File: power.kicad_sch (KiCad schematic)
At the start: 56 parts, among them J4 Conn_02x02_Counter_Clockwise, Q3 Q_NMOS, Q4 Q_NMOS, Q5 Q_NMOS, Q6 Q_NMOS, U10 CJ431, U6 TPS5430DDA, U7 TPS56A37, U8 TPS2121, U9 LDL212PV33R

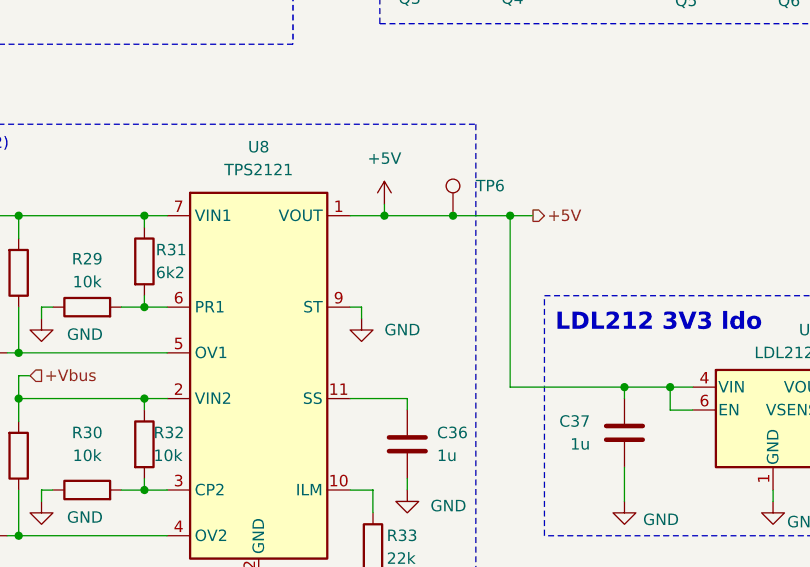
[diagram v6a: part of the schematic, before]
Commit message: schem: connect TPS2121 ST pin to MCU
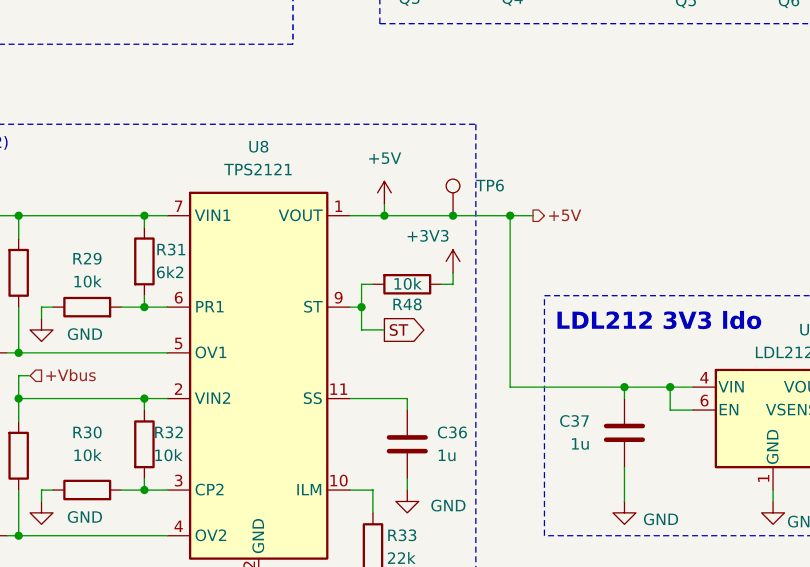
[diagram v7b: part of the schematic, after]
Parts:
- added R48: 10k, Resistor_SMD:R_0402_1005Metric, symbol Device:R
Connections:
- net +3V3: now also R48.1
- net GND: no longer U8.9 (ST)
- new net ST: R48.2, U8.9 (ST)
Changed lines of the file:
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@@
 	)
 	(junction
+		(at 172.72 96.52)
+		(diameter 0)
+		(color 0 0 0 0)
+	)
+	(junction
 		(at 148.59 106.68)
 		(diameter 0)
@@
 	(wire
 		(pts
-			(xy 171.45 96.52) (xy 172.72 96.52)
+			(xy 172.72 96.52) (xy 172.72 93.98)
 		)
 		(stroke
@@
 	(wire
 		(pts
+			(xy 181.61 93.98) (xy 182.88 93.98)
+		)
+		(stroke
+			(width 0)
+			(type default)
+		)
+	)
+	(wire
+		(pts
 			(xy 102.87 115.57) (xy 102.87 116.84)
 		)
@@
 	(wire
 		(pts
+			(xy 172.72 96.52) (xy 171.45 96.52)
+		)
+		(stroke
+			(width 0)
+			(type default)
+		)
+	)
+	(wire
+		(pts
 			(xy 125.73 101.6) (xy 124.46 101.6)
 		)
@@
 	(wire
 		(pts
+			(xy 182.88 93.98) (xy 182.88 92.71)
+		)
+		(stroke
+			(width 0)
+			(type default)
+		)
+	)
+	(wire
+		(pts
 			(xy 170.18 35.56) (xy 170.18 59.69)
 		)
@@
 	(wire
 		(pts
+			(xy 175.26 99.06) (xy 172.72 99.06)
+		)
+		(stroke
+			(width 0)
+			(type default)
+		)
+	)
+	(wire
+		(pts
 			(xy 134.62 104.14) (xy 134.62 106.68)
 		)
@@
 	(wire
 		(pts
-			(xy 93.98 43.18) (xy 95.25 43.18)
+			(xy 172.72 93.98) (xy 173.99 93.98)
 		)
 		(stroke
@@
 	(wire
 		(pts
-			(xy 248.92 105.41) (xy 252.73 105.41)
+			(xy 93.98 43.18) (xy 95.25 43.18)
 		)
 		(stroke
@@
 	(wire
 		(pts
-			(xy 95.25 43.18) (xy 99.06 43.18)
+			(xy 248.92 105.41) (xy 252.73 105.41)
 		)
 		(stroke
@@
 	(wire
 		(pts
-			(xy 222.25 34.29) (xy 222.25 35.56)
+			(xy 95.25 43.18) (xy 99.06 43.18)
 		)
 		(stroke
@@
 	(wire
 		(pts
-			(xy 60.96 101.6) (xy 71.12 101.6)
+			(xy 222.25 34.29) (xy 222.25 35.56)
 		)
 		(stroke
@@
 	(wire
 		(pts
-			(xy 74.93 96.52) (xy 74.93 97.79)
+			(xy 60.96 101.6) (xy 71.12 101.6)
 		)
 		(stroke
@@
 	(wire
 		(pts
-			(xy 172.72 96.52) (xy 172.72 97.79)
+			(xy 74.93 96.52) (xy 74.93 97.79)
 		)
 		(stroke
@@
 	(wire
 		(pts
+			(xy 172.72 96.52) (xy 172.72 99.06)
+		)
+		(stroke
+			(width 0)
+			(type default)
+		)
+	)
+	(wire
+		(pts
 			(xy 173.99 119.38) (xy 173.99 116.84)
 		)
@@
 		)
 	)
+	(global_label "ST"
+		(shape output)
+		(at 175.26 99.06 0)
+		(fields_autoplaced yes)
+		(effects
+			(font
+				(size 1.27 1.27)
+			)
+			(justify left)
+		)
+		(property "Intersheetrefs" "${INTERSHEET_REFS}"
+			(at 180.4223 99.06 0)
+			(effects
+				(font
+					(size 1.27 1.27)
+				)
+				(justify left)
+				(hide yes)
+			)
+		)
+	)
 	(hierarchical_label "+Vin"
 		(shape input)
@@
 	(symbol
 		(lib_id "power:GND")
-		(at 172.72 97.79 0)
-		(unit 1)
-		(exclude_from_sim no)
-		(in_bom yes)
-		(on_board yes)
-		(dnp no)
-		(fields_autoplaced yes)
-		(property "Reference" "#PWR069"
-			(at 172.72 104.14 0)
-			(effects
-				(font
-					(size 1.27 1.27)
-				)
-				(hide yes)
-			)
-		)
-		(property "Value" "GND"
-			(at 175.26 99.0599 0)
-			(effects
-				(font
-					(size 1.27 1.27)
-				)
-				(justify left)
-			)
-		)
-		(property "Footprint" ""
-			(at 172.72 97.79 0)
-			(effects
-				(font
-					(size 1.27 1.27)
-				)
-				(hide yes)
-			)
-		)
-		(property "Datasheet" ""
-			(at 172.72 97.79 0)
-			(effects
-				(font
-					(size 1.27 1.27)
-				)
-				(hide yes)
-			)
-		)
-		(property "Description" "Power symbol creates a global label with name \"GND\" , ground"
-			(at 172.72 97.79 0)
-			(effects
-				(font
-					(size 1.27 1.27)
-				)
-				(hide yes)
-			)
-		)
-		(pin "1"
-		)
-		(instances
-			(project "power"
-				(path "/1e5fa1ef-e283-4594-971e-80ab15cefa9e"
-					(reference "#PWR?")
-					(unit 1)
-				)
-			)
-			(project "motor-power-poc"
-				(path "/a1dc4c9e-7b20-4b66-a693-9133bc644c6b/c6ffff07-df24-4c45-882d-f55b522e3469"
-					(reference "#PWR069")
-					(unit 1)
-				)
-			)
-		)
-	)
-	(symbol
-		(lib_id "power:GND")
 		(at 125.73 49.53 0)
 		(unit 1)
@@
 	)
 	(symbol
+		(lib_id "power:+3V3")
+		(at 182.88 92.71 0)
+		(unit 1)
+		(exclude_from_sim no)
+		(in_bom yes)
+		(on_board yes)
+		(dnp no)
+		(property "Reference" "#PWR069"
+			(at 182.88 96.52 0)
+			(effects
+				(font
+					(size 1.27 1.27)
+				)
+				(hide yes)
+			)
+		)
+		(property "Value" "+3V3"
+			(at 180.086 88.646 0)
+			(effects
+				(font
+					(size 1.27 1.27)
+				)
+			)
+		)
+		(property "Footprint" ""
+			(at 182.88 92.71 0)
+			(effects
+				(font
+					(size 1.27 1.27)
+				)
+				(hide yes)
+			)
+		)
+		(property "Datasheet" ""
+			(at 182.88 92.71 0)
+			(effects
+				(font
+					(size 1.27 1.27)
+				)
+				(hide yes)
+			)
+		)
+		(property "Description" "Power symbol creates a global label with name \"+3V3\""
+			(at 182.88 92.71 0)
+			(effects
+				(font
+					(size 1.27 1.27)
+				)
+				(hide yes)
+			)
+		)
+		(pin "1"
+		)
+		(instances
+			(project "motor-power-poc"
+				(path "/a1dc4c9e-7b20-4b66-a693-9133bc644c6b/c6ffff07-df24-4c45-882d-f55b522e3469"
+					(reference "#PWR069")
+					(unit 1)
+				)
+			)
+		)
+	)
+	(symbol
 		(lib_id "Device:R")
 		(at 102.87 111.76 0)
@@
 					(unit 1)
 				)
+			)
+		)
+	)
+	(symbol
+		(lib_id "Device:R")
+		(at 177.8 93.98 270)
+		(unit 1)
+		(exclude_from_sim no)
+		(in_bom yes)
+		(on_board yes)
+		(dnp no)
+		(property "Reference" "R48"
+			(at 177.8 96.266 90)
+			(effects
+				(font
+					(size 1.27 1.27)
+				)
+			)
+		)
+		(property "Value" "10k"
+			(at 177.8 93.98 90)
+			(effects
+				(font
+					(size 1.27 1.27)
+				)
+			)
+		)
+		(property "Footprint" "Resistor_SMD:R_0402_1005Metric"
+			(at 177.8 92.202 90)
+			(effects
+				(font
+					(size 1.27 1.27)
+				)
+				(hide yes)
+			)
+		)
+		(property "Datasheet" "~"
+			(at 177.8 93.98 0)
+			(effects
+				(font
+					(size 1.27 1.27)
+				)
+				(hide yes)
+			)
+		)
+		(property "Description" "Resistor"
+			(at 177.8 93.98 0)
+			(effects
+				(font
+					(size 1.27 1.27)
+				)
+				(hide yes)
+			)
+		)
+		(property "Basic" "Y"
+			(at 177.8 93.98 0)
+			(effects
+				(font
+					(size 1.27 1.27)
+				)
+				(hide yes)
+			)
+		)
+		(property "JLCPCB Part #" "C25744"
+			(at 177.8 93.98 0)
+			(effects
+				(font
+					(size 1.27 1.27)
+				)
+				(hide yes)
+			)
+		)
+		(property "Manufacturer" "Uniroyal Elec"
+			(at 177.8 93.98 0)
+			(effects
+				(font
+					(size 1.27 1.27)
+				)
+				(hide yes)
+			)
+		)
+		(property "Manufacturer Part Number" "0402WGF1002TCE"
+			(at 177.8 93.98 0)
+			(effects
+				(font
+					(size 1.27 1.27)
+				)
+				(hide yes)
+			)
+		)
+		(pin "1"
+		)
+		(pin "2"
+		)
+		(instances
+			(project "motor-power-poc"
+				(path "/a1dc4c9e-7b20-4b66-a693-9133bc644c6b/c6ffff07-df24-4c45-882d-f55b522e3469"
+					(reference "R48")
+					(unit 1)
+				)

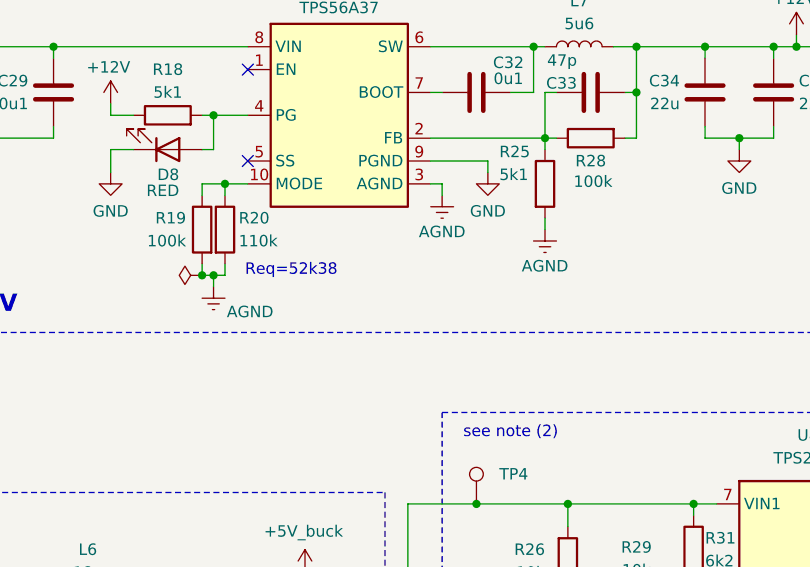
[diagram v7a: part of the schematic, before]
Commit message: schem: add AGND PGND net tie
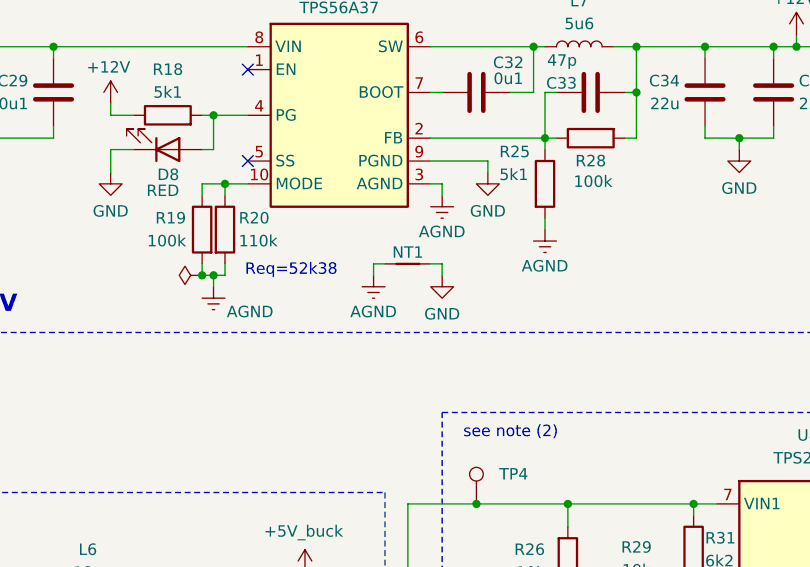
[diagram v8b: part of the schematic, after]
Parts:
- added NT1: NetTie_2, NetTie:NetTie-2_SMD_Pad0.5mm, symbol Device:NetTie_2
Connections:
- net AGND: now also NT1.1
- net GND: now also NT1.2
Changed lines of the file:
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@@
 	(wire
 		(pts
+			(xy 119.38 59.69) (xy 120.65 59.69)
+		)
+		(stroke
+			(width 0)
+			(type default)
+		)
+	)
+	(wire
+		(pts
 			(xy 97.79 115.57) (xy 62.23 115.57)
 		)
@@
 	(wire
 		(pts
+			(xy 113.03 60.96) (xy 113.03 59.69)
+		)
+		(stroke
+			(width 0)
+			(type default)
+		)
+	)
+	(wire
+		(pts
 			(xy 120.65 50.8) (xy 119.38 50.8)
 		)
@@
 	(wire
 		(pts
+			(xy 120.65 59.69) (xy 120.65 60.96)
+		)
+		(stroke
+			(width 0)
+			(type default)
+		)
+	)
+	(wire
+		(pts
 			(xy 195.58 33.02) (xy 195.58 35.56)
 		)
@@
 	(wire
 		(pts
+			(xy 113.03 59.69) (xy 114.3 59.69)
+		)
+		(stroke
+			(width 0)
+			(type default)
+		)
+	)
+	(wire
+		(pts
 			(xy 248.92 105.41) (xy 252.73 105.41)
 		)
@@
 	)
 	(symbol
+		(lib_id "power:GNDREF")
+		(at 113.03 60.96 0)
+		(unit 1)
+		(exclude_from_sim no)
+		(in_bom yes)
+		(on_board yes)
+		(dnp no)
+		(property "Reference" "#PWR090"
+			(at 113.03 67.31 0)
+			(effects
+				(font
+					(size 1.27 1.27)
+				)
+				(hide yes)
+			)
+		)
+		(property "Value" "AGND"
+			(at 113.03 65.024 0)
+			(effects
+				(font
+					(size 1.27 1.27)
+				)
+			)
+		)
+		(property "Footprint" ""
+			(at 113.03 60.96 0)
+			(effects
+				(font
+					(size 1.27 1.27)
+				)
+				(hide yes)
+			)
+		)
+		(property "Datasheet" ""
+			(at 113.03 60.96 0)
+			(effects
+				(font
+					(size 1.27 1.27)
+				)
+				(hide yes)
+			)
+		)
+		(property "Description" "Power symbol creates a global label with name \"GNDREF\" , reference supply ground"
+			(at 113.03 60.96 0)
+			(effects
+				(font
+					(size 1.27 1.27)
+				)
+				(hide yes)
+			)
+		)
+		(pin "1"
+		)
+		(instances
+			(project "motor-power-poc"
+				(path "/a1dc4c9e-7b20-4b66-a693-9133bc644c6b/c6ffff07-df24-4c45-882d-f55b522e3469"
+					(reference "#PWR090")
+					(unit 1)
+				)
+			)
+		)
+	)
+	(symbol
 		(lib_id "Regulator_Switching:TPS5430DDA")
 		(at 48.26 101.6 0)
@@
 	)
 	(symbol
+		(lib_id "Device:NetTie_2")
+		(at 116.84 59.69 0)
+		(unit 1)
+		(exclude_from_sim no)
+		(in_bom no)
+		(on_board yes)
+		(dnp no)
+		(property "Reference" "NT1"
+			(at 116.84 58.42 0)
+			(effects
+				(font
+					(size 1.27 1.27)
+				)
+			)
+		)
+		(property "Value" "NetTie_2"
+			(at 116.84 57.15 0)
+			(effects
+				(font
+					(size 1.27 1.27)
+				)
+				(hide yes)
+			)
+		)
+		(property "Footprint" "NetTie:NetTie-2_SMD_Pad0.5mm"
+			(at 116.84 59.69 0)
+			(effects
+				(font
+					(size 1.27 1.27)
+				)
+				(hide yes)
+			)
+		)
+		(property "Datasheet" "~"
+			(at 116.84 59.69 0)
+			(effects
+				(font
+					(size 1.27 1.27)
+				)
+				(hide yes)
+			)
+		)
+		(property "Description" "Net tie, 2 pins"
+			(at 116.84 59.69 0)
+			(effects
+				(font
+					(size 1.27 1.27)
+				)
+				(hide yes)
+			)
+		)
+		(pin "2"
+		)
+		(pin "1"
+		)
+		(instances
+			(project ""
+				(path "/a1dc4c9e-7b20-4b66-a693-9133bc644c6b/c6ffff07-df24-4c45-882d-f55b522e3469"
+					(reference "NT1")
+					(unit 1)
+				)
+			)
+		)
+	)
+	(symbol
 		(lib_id "Connector:TestPoint")
 		(at 124.46 86.36 0)
@@
 					(unit 1)
 				)
+			)
+		)
+	)
+	(symbol
+		(lib_id "power:GND")
+		(at 120.65 60.96 0)
+		(unit 1)
+		(exclude_from_sim no)
+		(in_bom yes)
+		(on_board yes)
+		(dnp no)
+		(property "Reference" "#PWR091"
+			(at 120.65 67.31 0)
+			(effects
+				(font
+					(size 1.27 1.27)
+				)
+				(hide yes)
+			)
+		)
+		(property "Value" "GND"
+			(at 120.65 65.278 0)
+			(effects
+				(font
+					(size 1.27 1.27)
+				)
+			)
+		)
+		(property "Footprint" ""
+			(at 120.65 60.96 0)
+			(effects
+				(font
+					(size 1.27 1.27)
+				)
+				(hide yes)
+			)
+		)
+		(property "Datasheet" ""
+			(at 120.65 60.96 0)
+			(effects
+				(font
+					(size 1.27 1.27)
+				)
+				(hide yes)
+			)
+		)
+		(property "Description" "Power symbol creates a global label with name \"GND\" , ground"
+			(at 120.65 60.96 0)
+			(effects
+				(font
+					(size 1.27 1.27)
+				)
+				(hide yes)
+			)
+		)
+		(pin "1"
+		)
+		(instances
+			(project "motor-power-poc"
+				(path "/a1dc4c9e-7b20-4b66-a693-9133bc644c6b/c6ffff07-df24-4c45-882d-f55b522e3469"
+					(reference "#PWR091")
+					(unit 1)
+				)
